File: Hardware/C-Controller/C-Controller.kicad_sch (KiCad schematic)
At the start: 22 parts, among them J1 Conn_01x02, J2 Conn_01x04, J3 Conn_01x06, J4 Conn_01x07, J5 Conn_01x05, U1 STM32L031K6Tx, Y1 32.786 kHz

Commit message: 1mm pitch headers
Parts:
- J2: footprint Connector_PinSocket_1.27mm:PinSocket_1x04_P1.27mm_Vertical -> Connector_PinSocket_1.00mm:PinSocket_1x04_P1.00mm_Vertical
- J3: footprint Connector_PinSocket_1.27mm:PinSocket_1x06_P1.27mm_Vertical -> Connector_PinSocket_1.00mm:PinSocket_1x06_P1.00mm_Vertical
- J4: footprint Connector_PinSocket_1.27mm:PinSocket_1x07_P1.27mm_Vertical -> Connector_PinSocket_1.00mm:PinSocket_1x07_P1.00mm_Vertical
- J5: footprint Connector_PinSocket_1.27mm:PinSocket_1x05_P1.27mm_Vertical -> Connector_PinSocket_1.00mm:PinSocket_1x05_P1.00mm_Vertical
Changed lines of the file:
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@@
   (symbol (lib_id "power:+3V3") (at 138.43 72.39 0) (unit 1)
     (in_bom yes) (on_board yes) (fields_autoplaced)
-    (property "Reference" "#PWR?" (id 0) (at 138.43 76.2 0)
+    (property "Reference" "#PWR0119" (id 0) (at 138.43 76.2 0)
       (effects (font (size 1.27 1.27)) hide)
     )
@@
       (effects (font (size 1.27 1.27)) (justify left))
     )
-    (property "Footprint" "Connector_PinSocket_1.27mm:PinSocket_1x05_P1.27mm_Vertical" (id 2) (at 138.43 151.13 0)
+    (property "Footprint" "Connector_PinSocket_1.00mm:PinSocket_1x05_P1.00mm_Vertical" (id 2) (at 138.43 151.13 0)
       (effects (font (size 1.27 1.27)) hide)
     )
@@
       (effects (font (size 1.27 1.27)) (justify left))
     )
-    (property "Footprint" "Connector_PinSocket_1.27mm:PinSocket_1x06_P1.27mm_Vertical" (id 2) (at 121.92 119.38 0)
+    (property "Footprint" "Connector_PinSocket_1.00mm:PinSocket_1x06_P1.00mm_Vertical" (id 2) (at 121.92 119.38 0)
       (effects (font (size 1.27 1.27)) hide)
     )
@@
       (effects (font (size 1.27 1.27)) (justify left))
     )
-    (property "Footprint" "Connector_PinSocket_1.27mm:PinSocket_1x07_P1.27mm_Vertical" (id 2) (at 160.02 129.54 0)
+    (property "Footprint" "Connector_PinSocket_1.00mm:PinSocket_1x07_P1.00mm_Vertical" (id 2) (at 160.02 129.54 0)
       (effects (font (size 1.27 1.27)) hide)
     )
@@
       (effects (font (size 1.27 1.27)) (justify left))
     )
-    (property "Footprint" "Connector_PinSocket_1.27mm:PinSocket_1x04_P1.27mm_Vertical" (id 2) (at 160.02 106.68 0)
+    (property "Footprint" "Connector_PinSocket_1.00mm:PinSocket_1x04_P1.00mm_Vertical" (id 2) (at 160.02 106.68 0)
       (effects (font (size 1.27 1.27)) hide)
     )
@@
     )
     (path "/6c7c0dab-a51d-4169-bd4a-58c378a84e63"
-      (reference "#PWR?") (unit 1) (value "+3V3") (footprint "")
+      (reference "#PWR0119") (unit 1) (value "+3V3") (footprint "")
     )
     (path "/b6a787d5-c5e5-4506-b7ec-bdfd3b8b5f97"
@@
     )
     (path "/e0382348-d4a6-400f-bef2-c854e466f80d"
-      (reference "J2") (unit 1) (value "Conn_01x04") (footprint "Connector_PinSocket_1.27mm:PinSocket_1x04_P1.27mm_Vertical")
+      (reference "J2") (unit 1) (value "Conn_01x04") (footprint "Connector_PinSocket_1.00mm:PinSocket_1x04_P1.00mm_Vertical")
     )
     (path "/a9743590-45a9-4dd4-86d1-35035513914d"
-      (reference "J3") (unit 1) (value "Conn_01x06") (footprint "Connector_PinSocket_1.27mm:PinSocket_1x06_P1.27mm_Vertical")
+      (reference "J3") (unit 1) (value "Conn_01x06") (footprint "Connector_PinSocket_1.00mm:PinSocket_1x06_P1.00mm_Vertical")
     )
     (path "/c24f0be4-46de-4c30-a90a-91cd072bf2d6"
-      (reference "J4") (unit 1) (value "Conn_01x07") (footprint "Connector_PinSocket_1.27mm:PinSocket_1x07_P1.27mm_Vertical")
+      (reference "J4") (unit 1) (value "Conn_01x07") (footprint "Connector_PinSocket_1.00mm:PinSocket_1x07_P1.00mm_Vertical")
     )
     (path "/97337fcd-172a-44c0-986f-729f37cc3d5c"
-      (reference "J5") (unit 1) (value "Conn_01x05") (footprint "Connector_PinSocket_1.27mm:PinSocket_1x05_P1.27mm_Vertical")
+      (reference "J5") (unit 1) (value "Conn_01x05") (footprint "Connector_PinSocket_1.00mm:PinSocket_1x05_P1.00mm_Vertical")
     )
     (path "/b9da0bee-9ca4-4256-9832-eaed8a23a561"

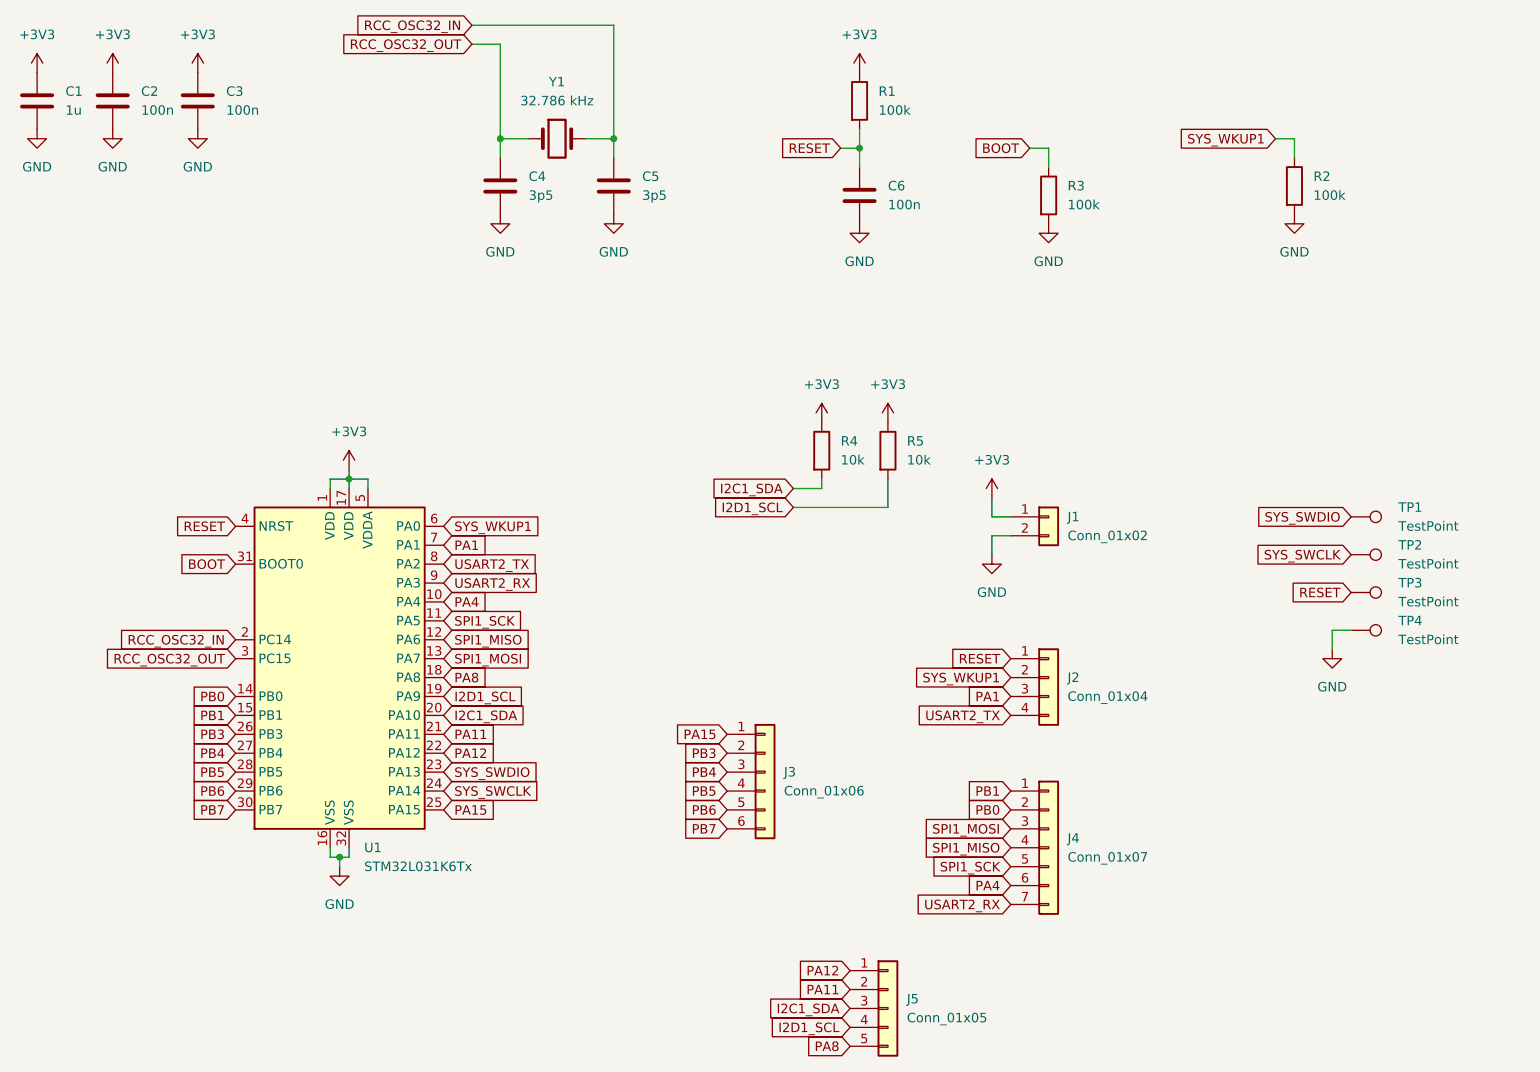
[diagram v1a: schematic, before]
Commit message: smaller components, crystal lib, status led, smaller board
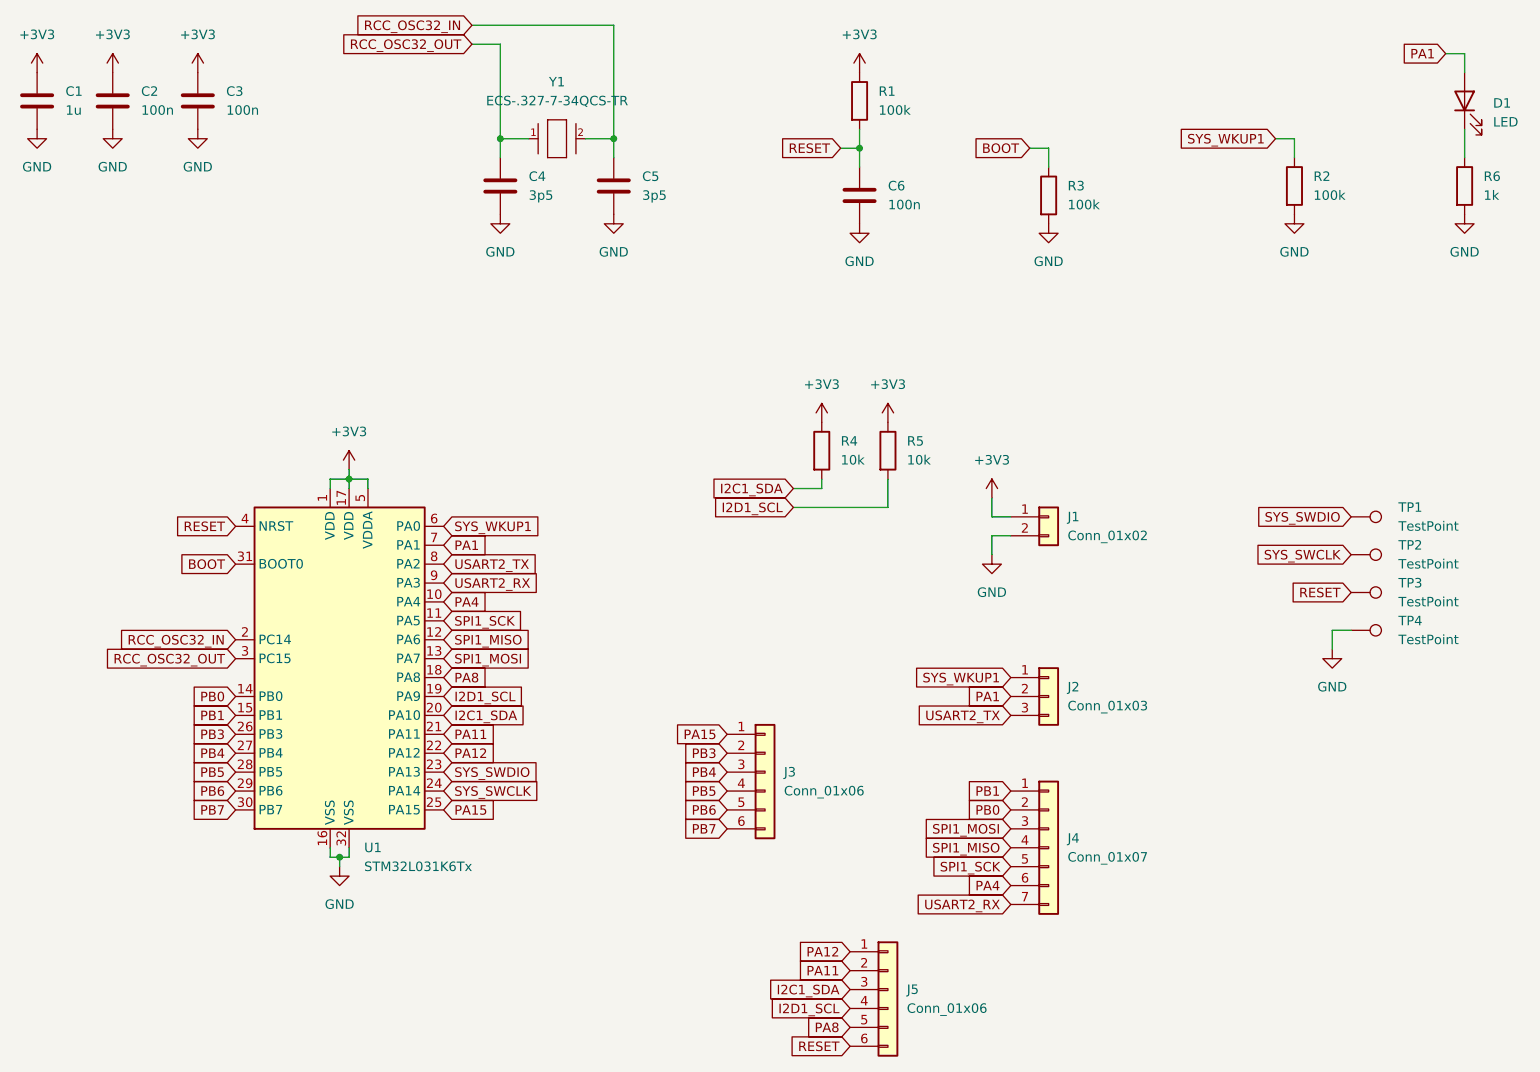
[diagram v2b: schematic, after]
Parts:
- removed J2: Conn_01x04, Connector_PinSocket_1.00mm:PinSocket_1x04_P1.00mm_Vertical, symbol Connector_Generic:Conn_01x04
- removed J5: Conn_01x05, Connector_PinSocket_1.00mm:PinSocket_1x05_P1.00mm_Vertical, symbol Connector_Generic:Conn_01x05
- removed Y1: 32.786 kHz, symbol Device:Crystal
- added D1: LED, LED_SMD:LED_0402_1005Metric, symbol Device:LED
- added J2: Conn_01x03, Connector_PinSocket_1.00mm:PinSocket_1x03_P1.00mm_Vertical, symbol Connector_Generic:Conn_01x03
- added J5: Conn_01x06, Connector_PinSocket_1.00mm:PinSocket_1x06_P1.00mm_Vertical, symbol Connector_Generic:Conn_01x06
- added R6: 1k, Resistor_SMD:R_0402_1005Metric, symbol Device:R
- added Y1: ECS-.327-7-34QCS-TR, Crys_ECS Inc._ECS-.327-7-34QCS-TR:ECS_Inc.-ECX-34Q-0-0-0, symbol eec:ECS-.327-7-34QCS-TR
- C2, C3, C6: footprint Capacitor_SMD:C_0603_1608Metric -> Capacitor_SMD:C_0402_1005Metric
- J1: footprint Connector_PinSocket_2.54mm:PinSocket_1x02_P2.54mm_Vertical -> Connector_PinSocket_2.00mm:PinSocket_1x02_P2.00mm_Vertical
- R1, R2, R3, R4, R5: footprint Resistor_SMD:R_0603_1608Metric -> Resistor_SMD:R_0402_1005Metric
- TP1, TP2, TP3, TP4: footprint TestPoint:TestPoint_Pad_D1.5mm -> TestPoint:TestPoint_Pad_D1.0mm
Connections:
- net GND: now also R6.2
- net I2C1_SDA: now also J5.3 (Pin_3)
- net I2D1_SCL: now also J5.4 (Pin_4)
- net PA1: now also D1.2 (A), J2.2 (Pin_2)
- net PA11: now also J5.2 (Pin_2)
- net PA12: now also J5.1 (Pin_1)
- net PA8: now also J5.5 (Pin_5)
- net RCC_OSC32_IN: now also Y1.2 (Out/In)
- net RCC_OSC32_OUT: now also Y1.1 (In/Out)
- net RESET: now also J5.6 (Pin_6)
- net SYS_WKUP1: now also J2.1 (Pin_1)
- net USART2_TX: now also J2.3 (Pin_3)
- new net: D1.1 (K), R6.1
